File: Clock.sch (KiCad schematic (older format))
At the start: 34 parts, among them SW1 SW_Push, SW2 SW_SPDT, U2 LM555, U3 LM555, U4 LM555, U5 74LS04, U6 74LS08, U7 74LS32, U8 74LS04, U9 74LS04

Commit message: Continued work.  Pushing for remote work.
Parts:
- removed U5, U8, U9: 74LS04, symbol 74xx:74LS04
- added U28: 74HC05, symbol 74xx:74HC04
- added unit 2 of U7
- U6: value 74LS08 -> 74HC08
- U7: value 74LS32 -> 74HC32
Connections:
- net CLK: now also U28.3
- net GND: now also U28.7 (GND)
- net VCC: now also U28.14 (VCC)
- net ~CLK: now also U28.4
- net at U3.3 (Q), U6.2: now also U28.1
- net at U6.5: now also U28.6
- net at U6.9: now also U28.2
- new net: U28.5, U7.6
- new net HALT_A: U7.4
- new net HALT_B: U7.5
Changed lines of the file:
@@
 $Descr A4 11693 8268
 encoding utf-8
-Sheet 7 8
+Sheet 5 9
 Title ""
 Date ""
@@
 P 6400 3950
 F 0 "U6" H 6400 4275 50  0000 C CNN
-F 1 "74LS08" H 6400 4184 50  0000 C CNN
+F 1 "74HC08" H 6400 4184 50  0000 C CNN
 F 2 "" H 6400 3950 50  0001 C CNN
 F 3 "http://www.ti.com/lit/gpn/sn74LS08" H 6400 3950 50  0001 C CNN
@@
 P 8450 4150
 F 0 "U6" H 8450 4475 50  0000 C CNN
-F 1 "74LS08" H 8450 4384 50  0000 C CNN
+F 1 "74HC08" H 8450 4384 50  0000 C CNN
 F 2 "" H 8450 4150 50  0001 C CNN
 F 3 "http://www.ti.com/lit/gpn/sn74LS08" H 8450 4150 50  0001 C CNN
@@
 P 6400 4850
 F 0 "U6" H 6400 5175 50  0000 C CNN
-F 1 "74LS08" H 6400 5084 50  0000 C CNN
+F 1 "74HC08" H 6400 5084 50  0000 C CNN
 F 2 "" H 6400 4850 50  0001 C CNN
 F 3 "http://www.ti.com/lit/gpn/sn74LS08" H 6400 4850 50  0001 C CNN
@@
 Wire Wire Line
 	5650 2650 5650 4050
-$Comp
-L 74xx:74LS04 U5
-U 1 1 5F16F551
-P 5650 4400
-F 0 "U5" V 5604 4580 50  0000 L CNN
-F 1 "74LS04" V 5695 4580 50  0000 L CNN
-F 2 "" H 5650 4400 50  0001 C CNN
-F 3 "http://www.ti.com/lit/gpn/sn74LS04" H 5650 4400 50  0001 C CNN
-	1    5650 4400
-	0    1    1    0
-$EndComp
 Wire Wire Line
 	5650 4700 5650 4750
@@
 P 7350 4050
 F 0 "U7" H 7350 4375 50  0000 C CNN
-F 1 "74LS32" H 7350 4284 50  0000 C CNN
+F 1 "74HC32" H 7350 4284 50  0000 C CNN
 F 2 "" H 7350 4050 50  0001 C CNN
 F 3 "http://www.ti.com/lit/gpn/sn74LS32" H 7350 4050 50  0001 C CNN
@@
 Wire Wire Line
 	6850 4150 7050 4150
-$Comp
-L 74xx:74LS04 U8
-U 1 1 5F195AC0
-P 7650 4650
-F 0 "U8" V 7604 4830 50  0000 L CNN
-F 1 "74LS04" V 7695 4830 50  0000 L CNN
-F 2 "" H 7650 4650 50  0001 C CNN
-F 3 "http://www.ti.com/lit/gpn/sn74LS04" H 7650 4650 50  0001 C CNN
-	1    7650 4650
-	1    0    0    -1
-$EndComp
-$Comp
-L 74xx:74LS04 U9
-U 1 1 5F1995EA
-P 9150 3800
-F 0 "U9" V 9104 3980 50  0000 L CNN
-F 1 "74LS04" V 9195 3980 50  0000 L CNN
-F 2 "" H 9150 3800 50  0001 C CNN
-F 3 "http://www.ti.com/lit/gpn/sn74LS04" H 9150 3800 50  0001 C CNN
-	1    9150 3800
-	1    0    0    -1
-$EndComp
-Wire Wire Line
-	7300 4650 7350 4650
-Wire Wire Line
-	7950 4650 8000 4650
-Wire Wire Line
-	8000 4650 8000 4250
+Wire Wire Line
+	7300 4900 7350 4900
+Wire Wire Line
+	8000 4350 8000 4250
 Wire Wire Line
 	8000 4250 8150 4250
@@
 P 3950 5950
 F 0 "U7" H 4180 5996 50  0000 L CNN
-F 1 "74LS32" H 4180 5905 50  0000 L CNN
+F 1 "74HC32" H 4180 5905 50  0000 L CNN
 F 2 "" H 3950 5950 50  0001 C CNN
 F 3 "http://www.ti.com/lit/gpn/sn74LS32" H 3950 5950 50  0001 C CNN
 	5    3950 5950
-	1    0    0    -1
-$EndComp
-$Comp
-L 74xx:74LS04 U5
-U 7 1 5F2068D5
-P 5250 5950
-F 0 "U5" H 5480 5996 50  0000 L CNN
-F 1 "74LS04" H 5480 5905 50  0000 L CNN
-F 2 "" H 5250 5950 50  0001 C CNN
-F 3 "http://www.ti.com/lit/gpn/sn74LS04" H 5250 5950 50  0001 C CNN
-	7    5250 5950
 	1    0    0    -1
 $EndComp
@@
 P 6550 5950
 F 0 "U6" H 6780 5996 50  0000 L CNN
-F 1 "74LS08" H 6780 5905 50  0000 L CNN
+F 1 "74HC08" H 6780 5905 50  0000 L CNN
 F 2 "" H 6550 5950 50  0001 C CNN
 F 3 "http://www.ti.com/lit/gpn/sn74LS08" H 6550 5950 50  0001 C CNN
@@
 Wire Wire Line
 	4600 5450 4600 5850
-Connection ~ 5250 5450
 Wire Wire Line
 	4600 6050 4600 6450
@@
 Wire Wire Line
 	5250 6500 5250 6450
-Connection ~ 5250 6450
 Wire Wire Line
 	3950 6500 3950 6450
@@
 	8000 3350 7250 3350
 Connection ~ 7250 3350
-Text HLabel 7300 4650 0    50   Input ~ 0
-HALT
+Text HLabel 7300 4900 0    50   Input ~ 0
+HALT_A
 Text HLabel 9500 4150 2    50   Input ~ 0
 CLK
@@
 Connection ~ 6550 2200
 Connection ~ 6550 2400
+$Comp
+L 74xx:74HC04 U28
+U 1 1 5F446CD2
+P 5650 4400
+F 0 "U28" V 5604 4580 50  0000 L CNN
+F 1 "74HC05" V 5695 4580 50  0000 L CNN
+F 2 "" H 5650 4400 50  0001 C CNN
+F 3 "https://assets.nexperia.com/documents/data-sheet/74HC_HCT04.pdf" H 5650 4400 50  0001 C CNN
+	1    5650 4400
+	0    1    1    0
+$EndComp
+$Comp
+L 74xx:74HC04 U28
+U 2 1 5F448193
+P 9150 3800
+F 0 "U28" H 9150 4117 50  0000 C CNN
+F 1 "74HC05" H 9150 4026 50  0000 C CNN
+F 2 "" H 9150 3800 50  0001 C CNN
+F 3 "https://assets.nexperia.com/documents/data-sheet/74HC_HCT04.pdf" H 9150 3800 50  0001 C CNN
+	2    9150 3800
+	1    0    0    -1
+$EndComp
+$Comp
+L 74xx:74HC04 U28
+U 3 1 5F448D9E
+P 8000 4650
+F 0 "U28" H 8000 4967 50  0000 C CNN
+F 1 "74HC05" H 8000 4876 50  0000 C CNN
+F 2 "" H 8000 4650 50  0001 C CNN
+F 3 "https://assets.nexperia.com/documents/data-sheet/74HC_HCT04.pdf" H 8000 4650 50  0001 C CNN
+	3    8000 4650
+	0    -1   -1   0
+$EndComp
+$Comp
+L 74xx:74HC04 U28
+U 7 1 5F449D6E
+P 5250 5950
+F 0 "U28" H 5480 5996 50  0000 L CNN
+F 1 "74HC05" H 5480 5905 50  0000 L CNN
+F 2 "" H 5250 5950 50  0001 C CNN
+F 3 "https://assets.nexperia.com/documents/data-sheet/74HC_HCT04.pdf" H 5250 5950 50  0001 C CNN
+	7    5250 5950
+	1    0    0    -1
+$EndComp
+Connection ~ 5250 5450
+Connection ~ 5250 6450
+Text HLabel 7300 5100 0    50   Input ~ 0
+HALT_B
+$Comp
+L 74xx:74LS32 U7
+U 2 1 5FB8BB70
+P 7650 5000
+F 0 "U7" V 7696 4820 50  0000 R CNN
+F 1 "74HC32" V 7605 4820 50  0000 R CNN
+F 2 "" H 7650 5000 50  0001 C CNN
+F 3 "http://www.ti.com/lit/gpn/sn74LS32" H 7650 5000 50  0001 C CNN
+	2    7650 5000
+	1    0    0    -1
+$EndComp
+Wire Wire Line
+	7350 5100 7300 5100
+Wire Wire Line
+	7950 5000 8000 5000
+Wire Wire Line
+	8000 5000 8000 4950
 $EndSCHEMATC

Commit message: Remote work
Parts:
- added R32, R33, R34: 10k, symbol Device:R
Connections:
- net VCC: now also R32.1, R33.2, R34.1
- net ~CLK: now also R34.2
- net at U28.6, U6.5: now also R33.1
- net at U28.2, U6.9: now also R32.2
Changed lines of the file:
@@
 	9450 3800 9500 3800
 Wire Wire Line
-	8800 4150 9500 4150
+	8800 4150 9600 4150
 Connection ~ 8800 4150
 $Comp
@@
 Text HLabel 7300 4900 0    50   Input ~ 0
 HALT_A
-Text HLabel 9500 4150 2    50   Input ~ 0
+Text HLabel 9600 4150 2    50   Input ~ 0
 CLK
-Text HLabel 9500 3800 2    50   Input ~ 0
+Text HLabel 9600 3800 2    50   Input ~ 0
 ~CLK
 Wire Wire Line
@@
 Wire Wire Line
 	8000 5000 8000 4950
+$Comp
+L Device:R R33
+U 1 1 5F465BE8
+P 8000 3850
+F 0 "R33" V 8207 3850 50  0000 C CNN
+F 1 "10k" V 8116 3850 50  0000 C CNN
+F 2 "" V 7930 3850 50  0001 C CNN
+F 3 "~" H 8000 3850 50  0001 C CNN
+	1    8000 3850
+	-1   0    0    1
+$EndComp
+$Comp
+L Device:R R34
+U 1 1 5F499312
+P 9500 3550
+F 0 "R34" V 9707 3550 50  0000 C CNN
+F 1 "10k" V 9616 3550 50  0000 C CNN
+F 2 "" V 9430 3550 50  0001 C CNN
+F 3 "~" H 9500 3550 50  0001 C CNN
+	1    9500 3550
+	1    0    0    -1
+$EndComp
+$Comp
+L Device:R R32
+U 1 1 5F49FD9C
+P 5400 4750
+F 0 "R32" V 5607 4750 50  0000 C CNN
+F 1 "10k" V 5516 4750 50  0000 C CNN
+F 2 "" V 5330 4750 50  0001 C CNN
+F 3 "~" H 5400 4750 50  0001 C CNN
+	1    5400 4750
+	0    -1   -1   0
+$EndComp
+Wire Wire Line
+	5550 4750 5650 4750
+Connection ~ 5650 4750
+Wire Wire Line
+	5250 4750 5200 4750
+Wire Wire Line
+	5200 4750 5200 4650
+Wire Wire Line
+	8000 4000 8000 4250
+Connection ~ 8000 4250
+Wire Wire Line
+	8000 3700 8000 3650
+Wire Wire Line
+	9500 3700 9500 3800
+Connection ~ 9500 3800
+Wire Wire Line
+	9500 3800 9600 3800
+Wire Wire Line
+	9500 3400 9500 3350
+$Comp
+L power:VCC #PWR091
+U 1 1 5F4D04D6
+P 9500 3350
+F 0 "#PWR091" H 9500 3200 50  0001 C CNN
+F 1 "VCC" H 9517 3523 50  0000 C CNN
+F 2 "" H 9500 3350 50  0001 C CNN
+F 3 "" H 9500 3350 50  0001 C CNN
+	1    9500 3350
+	1    0    0    -1
+$EndComp
+$Comp
+L power:VCC #PWR090
+U 1 1 5F4D183D
+P 8000 3650
+F 0 "#PWR090" H 8000 3500 50  0001 C CNN
+F 1 "VCC" H 8017 3823 50  0000 C CNN
+F 2 "" H 8000 3650 50  0001 C CNN
+F 3 "" H 8000 3650 50  0001 C CNN
+	1    8000 3650
+	1    0    0    -1
+$EndComp
+$Comp
+L power:VCC #PWR089
+U 1 1 5F4D8763
+P 5200 4650
+F 0 "#PWR089" H 5200 4500 50  0001 C CNN
+F 1 "VCC" H 5217 4823 50  0000 C CNN
+F 2 "" H 5200 4650 50  0001 C CNN
+F 3 "" H 5200 4650 50  0001 C CNN
+	1    5200 4650
+	1    0    0    -1
+$EndComp
 $EndSCHEMATC

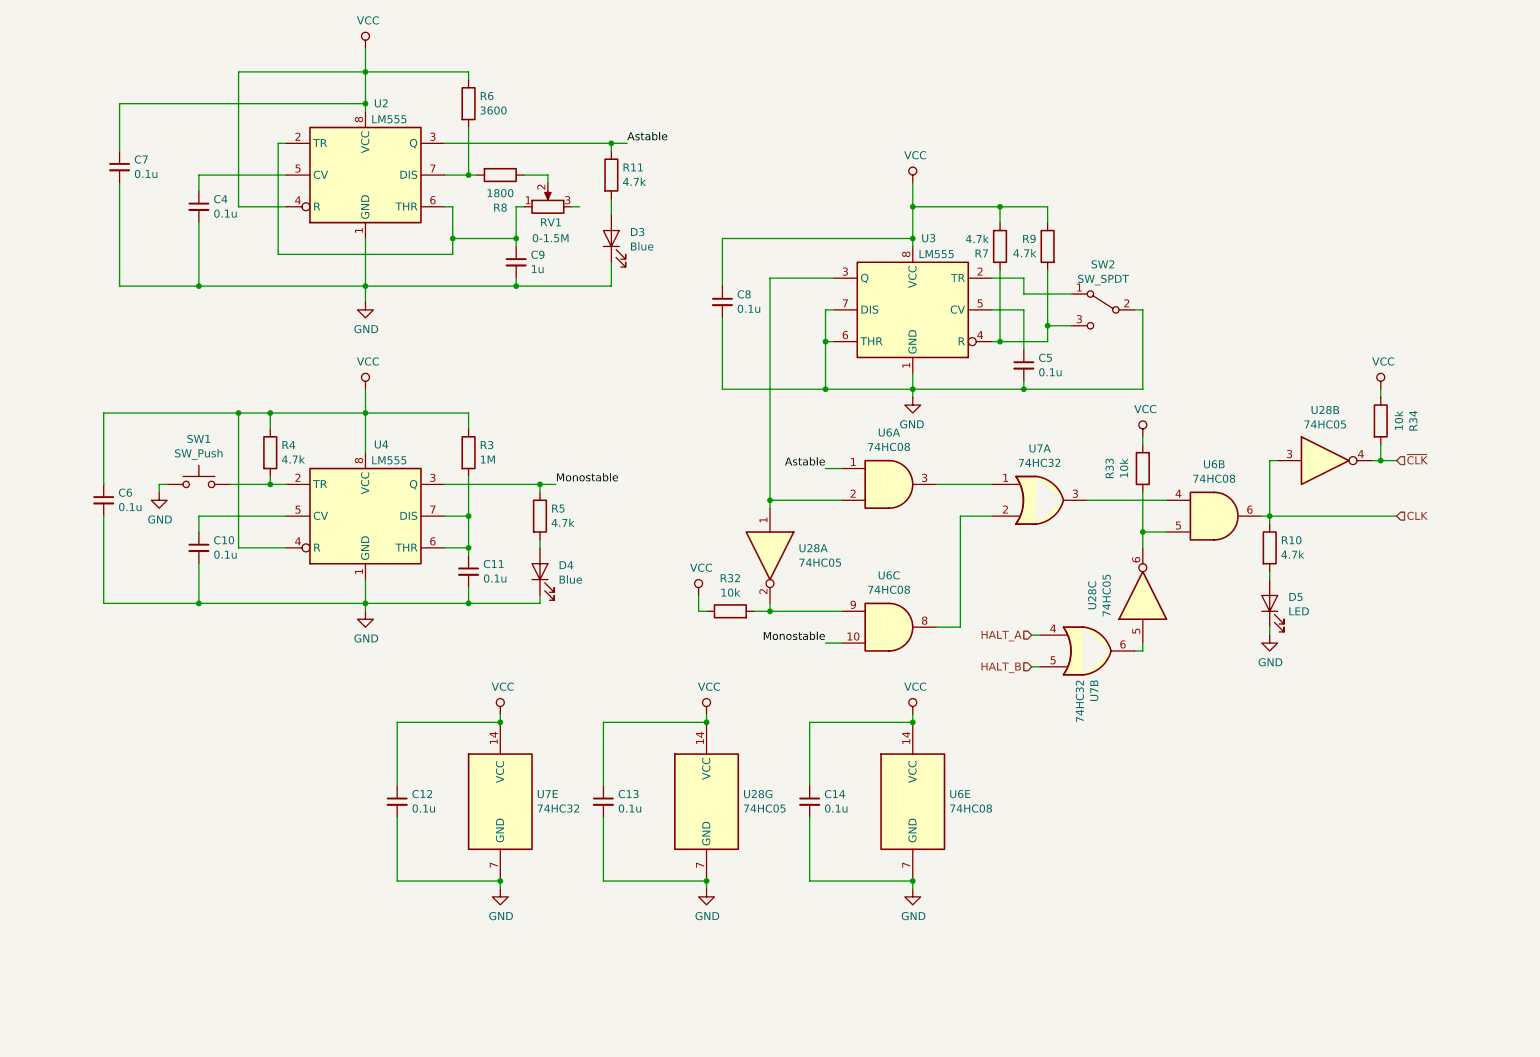
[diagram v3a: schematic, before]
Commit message: Migrated old device part numbers to SN74 LS or HCT series
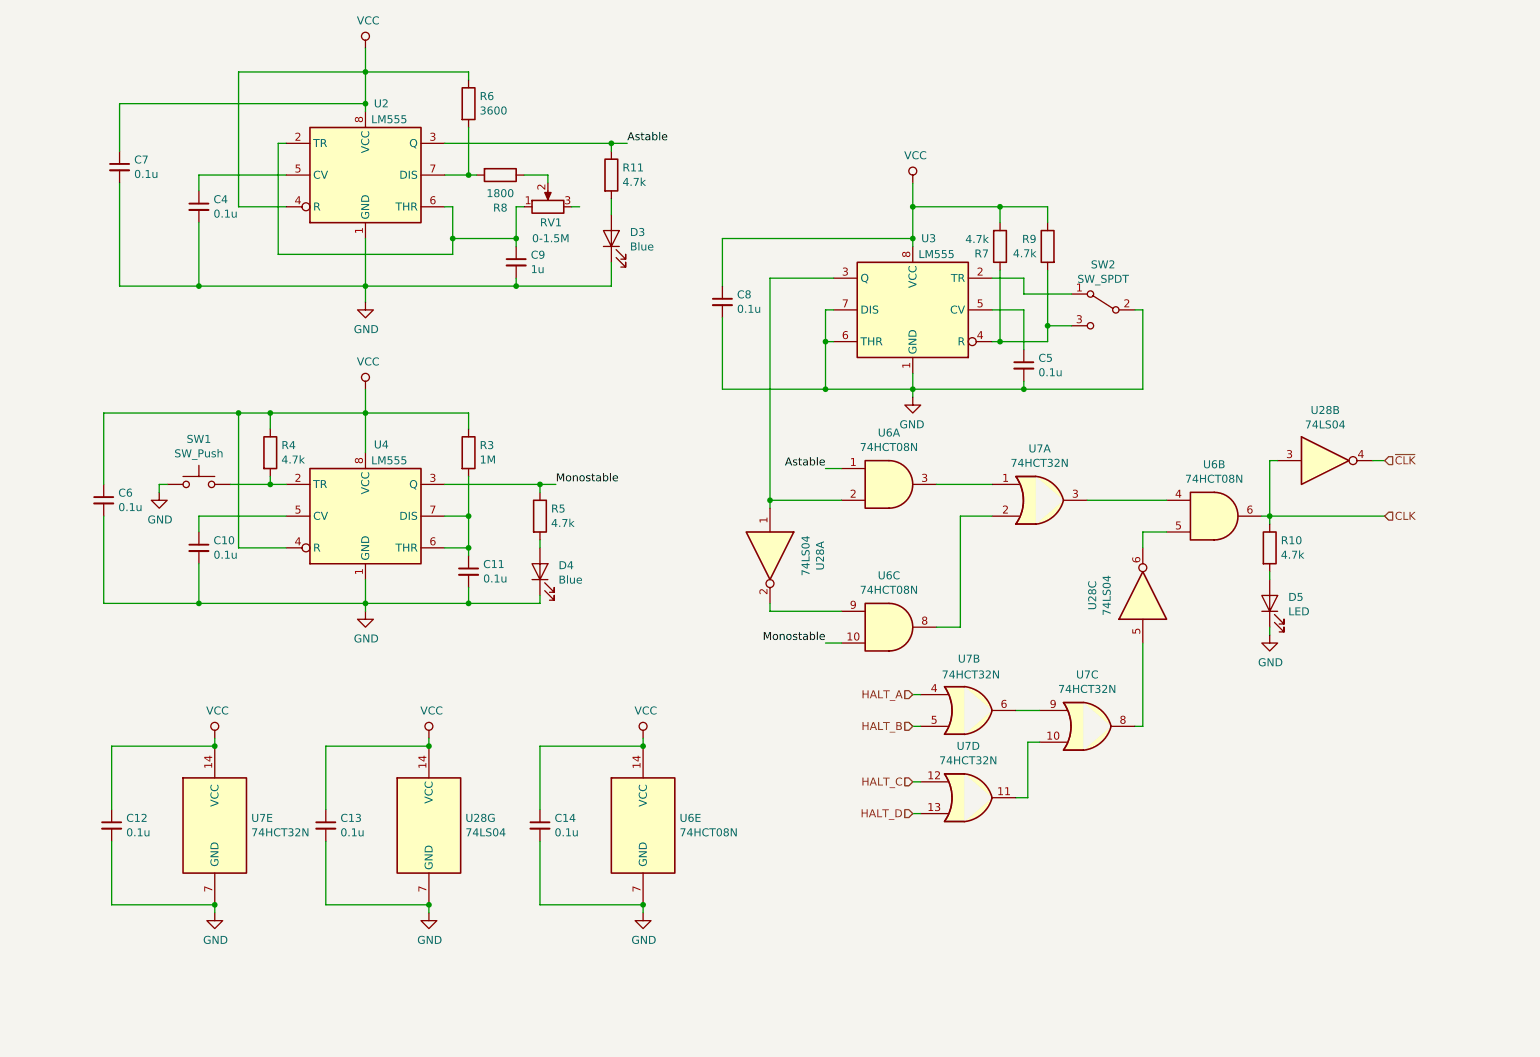
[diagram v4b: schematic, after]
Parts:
- removed R32, R33, R34: 10k, symbol Device:R
- removed U28: 74HC05, symbol 74xx:74HC04
- added U28: 74LS04, symbol 74xx:74LS04
- added unit 3 of U7
- added unit 4 of U7
- U6: value 74HC08 -> 74HCT08N
- U7: value 74HC32 -> 74HCT32N
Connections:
- net CLK: now also U28.3
- net GND: now also U28.7 (GND)
- net VCC: now also U28.14 (VCC)
- net ~CLK: now also U28.4
- net at U3.3 (Q), U6.2: now also U28.1
- net at U6.5: now also U28.6
- net at U6.9: now also U28.2
- net at U7.6: now also U7.9
- new net: U7.10, U7.11
- new net: U28.5, U7.8
- new net HALT_C: U7.12
- new net HALT_D: U7.13
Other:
- moved on the sheet: C12, C13, C14, U6E, U7B, U7E

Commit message: Remote work
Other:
- note added: "Astable clock"
- note added: "Astable or\nmonostable\nselector"
- note added: "HALT logic"
- note added: "Monostable button\npress"
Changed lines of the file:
@@
 Connection ~ 3500 5600
 Connection ~ 3500 6600
+Text Notes 5325 1625 2    118  ~ 0
+Astable clock
+Text Notes 875  3600 0    118  ~ 0
+Monostable button\npress
+Text Notes 8250 2275 2    118  ~ 0
+Astable or\nmonostable\nselector
+Text Notes 7750 6325 2    118  ~ 0
+HALT logic
 $EndSCHEMATC

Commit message: Replaced all broken schematics with the up-to-date versions.  Some symbols missing.  This version will be the one created IRL except for the carry flag.
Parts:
- removed C13, C14: 0.1u, symbol Device:C_Small
- removed SW2: SW_SPDT, symbol Switch:SW_SPDT
- removed U28: 74LS04, symbol 74xx:74LS04
- removed U6: 74HCT08N, symbol 74xx:74LS08
- added C306, C309: 0.1u, symbol Breadboard_CPU-rescue:C_Small-Device
- added R309: 100k, symbol Breadboard_CPU-rescue:R-Device
- added SW302: TOG_SRC, symbol Breadboard_CPU-rescue:SW_Push-Switch
- added U302: 74LS04, symbol Breadboard_CPU-rescue:74LS04-74xx
- added U305: 74HCT08N, symbol Breadboard_CPU-rescue:74LS08-74xx
- C301: renamed from C6; symbol Device:C_Small -> Breadboard_CPU-rescue:C_Small-Device
- C302: renamed from C12; symbol Device:C_Small -> Breadboard_CPU-rescue:C_Small-Device
- C303: renamed from C7; symbol Device:C_Small -> Breadboard_CPU-rescue:C_Small-Device
- C304: renamed from C4; symbol Device:C_Small -> Breadboard_CPU-rescue:C_Small-Device
- C305: renamed from C10; symbol Device:C_Small -> Breadboard_CPU-rescue:C_Small-Device
- C307: renamed from C11; symbol Device:C_Small -> Breadboard_CPU-rescue:C_Small-Device
- C308: renamed from C9; value 1u -> 4.7u; symbol Device:C_Small -> Breadboard_CPU-rescue:C_Small-Device
- C310: renamed from C5; symbol Device:C_Small -> Breadboard_CPU-rescue:C_Small-Device
- C311: renamed from C8; symbol Device:C_Small -> Breadboard_CPU-rescue:C_Small-Device
- D301: renamed from D4; symbol Device:LED -> Breadboard_CPU-rescue:LED-Device
- D302: renamed from D3; symbol Device:LED -> Breadboard_CPU-rescue:LED-Device
- D303: renamed from D5; symbol Device:LED -> Breadboard_CPU-rescue:LED-Device
- R301: renamed from R4; symbol Device:R -> Breadboard_CPU-rescue:R-Device
- R302: renamed from R6; value 3600 -> 1000; symbol Device:R -> Breadboard_CPU-rescue:R-Device
- R303: renamed from R3; symbol Device:R -> Breadboard_CPU-rescue:R-Device
- R304: renamed from R8; value 1800 -> 1000; symbol Device:R -> Breadboard_CPU-rescue:R-Device
- R305: renamed from R5; symbol Device:R -> Breadboard_CPU-rescue:R-Device
- R306: renamed from R11; symbol Device:R -> Breadboard_CPU-rescue:R-Device
- R307: renamed from R7; value 4.7k -> 10k; symbol Device:R -> Breadboard_CPU-rescue:R-Device
- R308: renamed from R9; value 4.7k -> 10k; symbol Device:R -> Breadboard_CPU-rescue:R-Device
- R310: renamed from R10; symbol Device:R -> Breadboard_CPU-rescue:R-Device
- RV301: renamed from RV1; value 0-1.5M -> 0-10k; symbol Device:R_POT -> Breadboard_CPU-rescue:R_POT-Device
- SW301: renamed from SW1; value SW_Push -> PULSE_CLK; symbol Switch:SW_Push -> Breadboard_CPU-rescue:SW_Push-Switch
- U301: renamed from U7; symbol 74xx:74LS32 -> Breadboard_CPU-rescue:74LS32-74xx
- U303: renamed from U2; symbol Timer:LM555 -> Breadboard_CPU-rescue:LM555-Timer
- U304: renamed from U4; symbol Timer:LM555 -> Breadboard_CPU-rescue:LM555-Timer
- U306: renamed from U3; symbol Timer:LM555 -> Breadboard_CPU-rescue:LM555-Timer
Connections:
- net Astable: now also U305.1
- net CLK: now also U302.1, U305.11
- net GND: now also R308.2, C306.2, C309.2, U302.7 (GND), U305.7 (GND); no longer U306.6 (THR), U306.7 (DIS)
- net Monostable: now also U305.5
- net VCC: now also R307.1, C306.1, C309.1, U302.14 (VCC), U305.14 (VCC); no longer C311.1, R307.2, R308.1
- net ~CLK: now also U302.2
- net at U306.2 (TR): now also R307.2, R308.1, U306.6 (THR), SW302.2
- net at U306.3 (Q): now also U306.4 (R), R309.2, U302.5, U305.2
- net at U301.1: now also U305.3
- net at U301.3: now also U305.12
- net at U301.2: now also U305.6
- net at U301.8: now also U302.3
- new net: C311.1, R309.1, SW302.1
- new net: U302.6, U305.4
- new net: U302.4, U305.13
- no-connect marks 0 -> 10
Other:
- moved on the sheet: C310, C311, R307, R308, U306
